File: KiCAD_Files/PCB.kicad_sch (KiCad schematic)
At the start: 33 parts, among them SW1 SW_Push, SW2 SW_Push, SW3 SW_Push, U1 NodeMCU_1.0_(ESP-12E), U2 LM35-LP

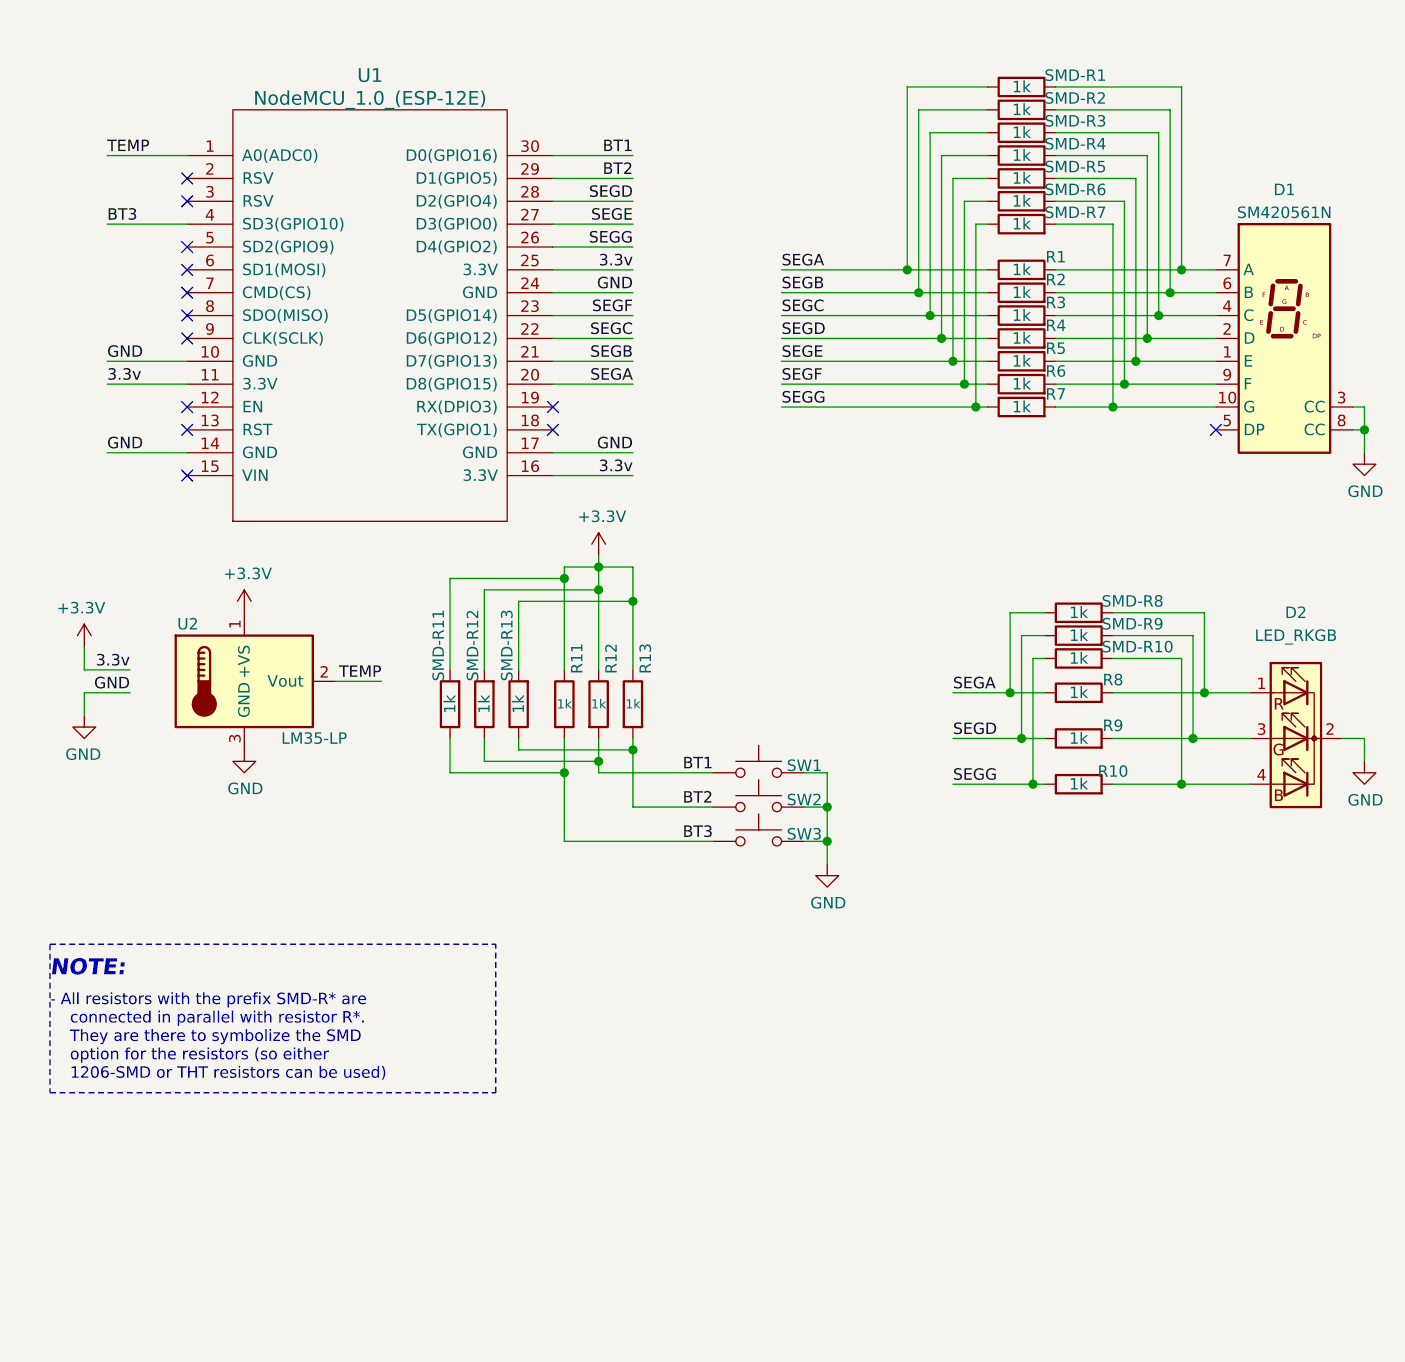
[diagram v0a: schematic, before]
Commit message: Started working on V1.1 of the PCB. Many more changes needed
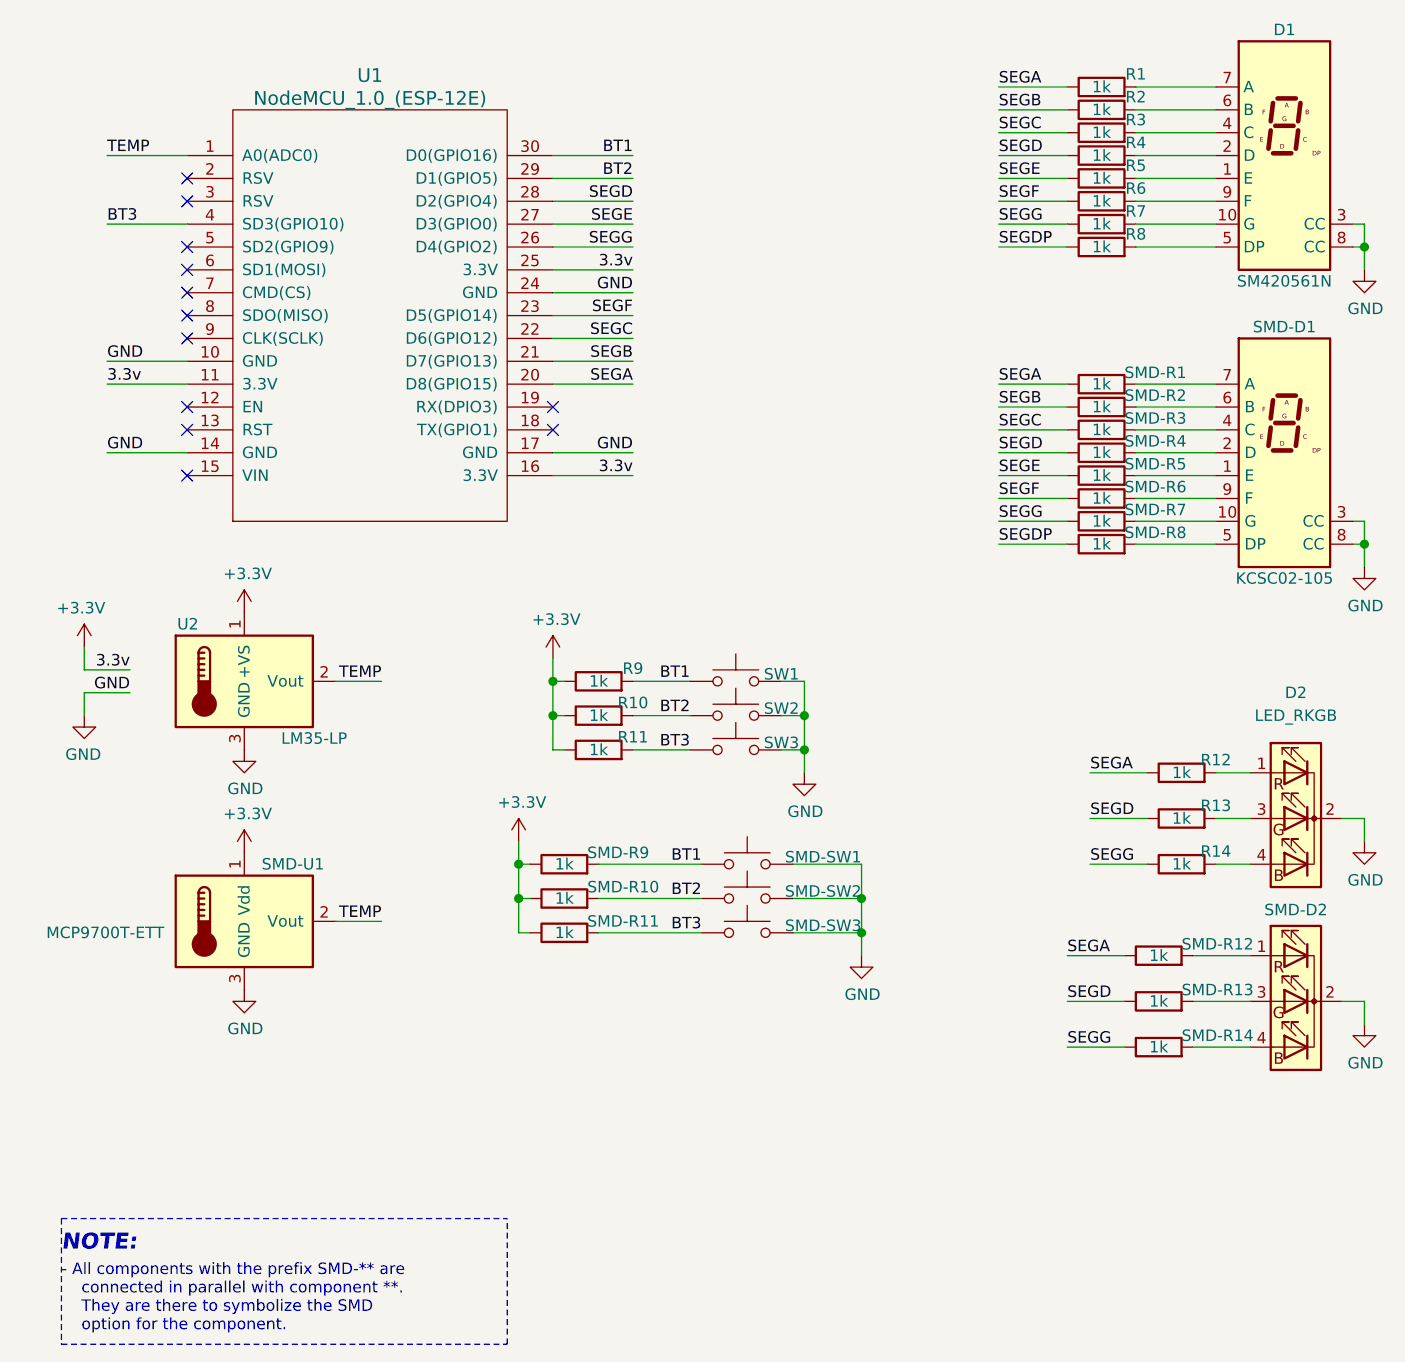
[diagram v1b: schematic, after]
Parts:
- removed R12, R13: 1k, Resistor_THT:R_Axial_DIN0207_L6.3mm_D2.5mm_P10.16mm_Horizontal, symbol Device:R
- added R10, R11: 1k, Resistor_THT:R_Axial_DIN0207_L6.3mm_D2.5mm_P10.16mm_Horizontal, symbol Device:R
- added R8: 1k, Resistor_THT:R_Axial_DIN0207_L6.3mm_D2.5mm_P7.62mm_Horizontal, symbol Device:R
- added SMD-D1: KCSC02-105, Display_7Segment:KCSC02-105, symbol Display_Character:KCSC02-105
- added SMD-D2: LED_RKGB, LED_THT:LED_D5.0mm-4_RGB_Staggered_Pins, symbol Device:LED_RKGB
- added SMD-R14: 1k, Resistor_SMD:R_1206_3216Metric_Pad1.30x1.75mm_HandSolder, symbol Device:R
- added SMD-SW1, SMD-SW2, SMD-SW3: SW_Push, Button_Switch_SMD:SW_Push_1P1T_NO_6x6mm_H9.5mm, symbol Switch:SW_Push
- added SMD-U1: MCP9700T-ETT, Package_TO_SOT_SMD:SOT-23, symbol Sensor_Temperature:MCP9700T-ETT
- renumbered R8 to R12, R9 to R13, R10 to R14, R11 to R9
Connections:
- net +3V3: now also SMD-R10.1, SMD-R11.1, SMD-R9.1, R10.1, R11.1, SMD-U1.1 (Vdd); no longer SMD-R11.2, SMD-R12.2, SMD-R13.2
- net BT1: now also R9.2, SMD-R9.2, SMD-SW1.1; no longer SMD-R12.1
- net BT2: now also SMD-R10.2, R10.2, SMD-SW2.1; no longer SMD-R13.1
- net BT3: now also SMD-R11.2, R11.2, SMD-SW3.1; no longer R9.2, SMD-R11.1
- net GND: now also SMD-D1.3 (CC), SMD-D1.8 (CC), SMD-D2.2 (K), SMD-SW1.2, SMD-SW2.2, SMD-SW3.2, SMD-U1.3 (GND)
- net SEGA: now also SMD-R12.1; no longer SMD-R8.1
- net SEGD: now also SMD-R13.1; no longer SMD-R9.1
- net SEGG: now also SMD-R14.1; no longer SMD-R10.1
- net TEMP: now also SMD-U1.2 (Vout)
- net at D1.1 (E), R5.2: no longer SMD-R5.2
- net at D1.10 (G), R7.2: no longer SMD-R7.2
- net at D1.2 (D), R4.2: no longer SMD-R4.2
- net at D1.4 (C), R3.2: no longer SMD-R3.2
- net at D1.5 (DP): now also R8.2
- net at D1.6 (B), R2.2: no longer SMD-R2.2
- net at D1.7 (A), R1.2: no longer SMD-R1.2
- net at D1.9 (F), R6.2: no longer SMD-R6.2
- net at D2.4 (BA), R14.2: no longer SMD-R10.2
- net at D2.1 (RA), R12.2: no longer SMD-R8.2
- net at D2.3 (GA), R13.2: no longer SMD-R9.2
- new net: SMD-D2.4 (BA), SMD-R14.2
- new net: SMD-D1.5 (DP), SMD-R8.2
- new net: SMD-D1.7 (A), SMD-R1.2
- new net: SMD-D1.10 (G), SMD-R7.2
- new net: SMD-D1.1 (E), SMD-R5.2
- new net: SMD-D1.2 (D), SMD-R4.2
- new net: SMD-D1.4 (C), SMD-R3.2
- new net: SMD-D1.6 (B), SMD-R2.2
- new net: SMD-D1.9 (F), SMD-R6.2
- new net: SMD-D2.1 (RA), SMD-R12.2
- new net: SMD-D2.3 (GA), SMD-R13.2
- new net SEGDP: R8.1, SMD-R8.1
- no-connect marks 13 -> 12
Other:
- note added: "- All components with the prefix SMD-** are connected in parallel with component **. They are there to symbolize the SMD option for the component."
- note removed: "- All resistors with the prefix SMD-R* are connected in parallel with resistor R*. They are there to symbolize the SMD option for the resistors (so either 1206-SMD or THT resistors can be used)"
- moved on the sheet: D1, D2, R1, R12, R13, R14, R2, R3, R4, R5, R6, R7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
